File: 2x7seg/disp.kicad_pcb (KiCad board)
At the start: 2 copper layers, 35.6 x 30.5 mm, 9 parts, among them P1 CONN_01X08, P2 CONN_01X08, U1 TLC59282

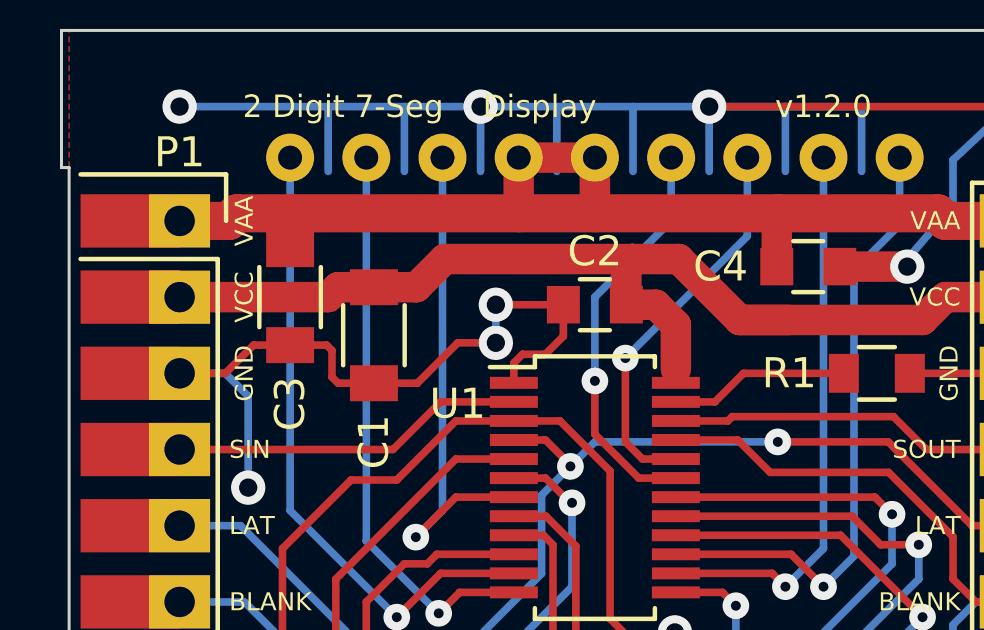
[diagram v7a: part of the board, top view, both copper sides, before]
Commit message: Move U1 reference designator. Upload to OSHPark.
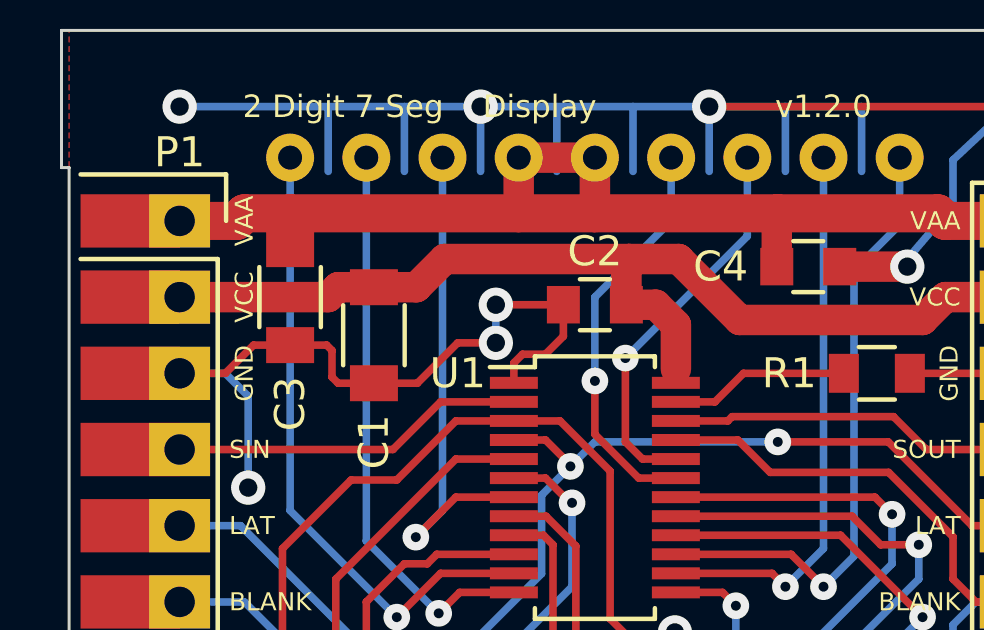
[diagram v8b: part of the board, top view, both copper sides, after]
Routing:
- net VCC: track 40.6 -> 38.9 mm
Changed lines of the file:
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@@
     (thickness 1.6)
     (drawings 35)
-    (tracks 289)
+    (tracks 286)
     (zones 0)
     (modules 9)
@@
   )
   (setup
-    (last_trace_width 0.254)
+    (last_trace_width 1.016)
     (user_trace_width 0.254)
     (user_trace_width 0.381)
@@
     (tags "SOIC 25mil")
     (attr smd)
-    (fp_text reference U1 (at -4.572 -2.794) (layer F.SilkS)
+    (fp_text reference U1 (at -4.572 -3.81) (layer F.SilkS)
       (effects (font (size 1 1) (thickness 0.15)))
     )
@@
   (gr_line (start 127 114.3) (end 162.56 114.3) (angle 90) (layer Edge.Cuts) (width 0.1))
   (gr_line (start 127.254 88.392) (end 127.254 109.728) (angle 90) (layer Edge.Cuts) (width 0.1))
+  (segment (start 139.77 91.44) (end 145.923 91.44) (width 1.016) (layer F.Cu) (net 1))
+  (segment (start 145.923 91.44) (end 147.574 91.44) (width 1.016) (layer F.Cu) (net 1))
+  (segment (start 145.83 92.964) (end 145.83 91.533) (width 1.016) (layer F.Cu) (net 1))
+  (segment (start 145.83 91.533) (end 145.923 91.44) (width 1.016) (layer F.Cu) (net 1))
+  (segment (start 137.414 92.38) (end 138.83 92.38) (width 1.016) (layer F.Cu) (net 1))
+  (segment (start 138.83 92.38) (end 139.77 91.44) (width 1.016) (layer F.Cu) (net 1))
+  (segment (start 147.574 91.44) (end 149.606 93.472) (width 1.016) (layer F.Cu) (net 1))
   (segment (start 149.606 93.472) (end 155.702 93.472) (width 1.016) (layer F.Cu) (net 1))
   (segment (start 155.702 93.472) (end 156.464 92.71) (width 1.016) (layer F.Cu) (net 1))
-  (segment (start 156.464 92.71) (end 160.655 92.71) (width 1.016) (layer F.Cu) (net 1) (status 20))
+  (segment (start 156.464 92.71) (end 160.655 92.71) (width 1.016) (layer F.Cu) (net 1))
   (segment (start 145.83 92.964) (end 146.812 92.964) (width 1.016) (layer F.Cu) (net 1) (status 10))
   (segment (start 146.812 92.964) (end 147.48 93.632) (width 1.016) (layer F.Cu) (net 1))
   (segment (start 147.48 93.632) (end 147.48 95.1135) (width 1.016) (layer F.Cu) (net 1))
-  (segment (start 145.83 92.964) (end 145.83 91.64002) (width 1.016) (layer F.Cu) (net 1) (status 10))
-  (segment (start 145.83 91.64002) (end 146.03002 91.44) (width 1.016) (layer F.Cu) (net 1))
   (segment (start 128.905 92.71) (end 135.89 92.71) (width 1.016) (layer F.Cu) (net 1) (status 10))
   (segment (start 135.89 92.71) (end 136.22 92.38) (width 1.016) (layer F.Cu) (net 1))
   (segment (start 136.22 92.38) (end 137.414 92.38) (width 1.016) (layer F.Cu) (net 1) (status 20))
-  (segment (start 137.414 92.38) (end 138.83 92.38) (width 1.016) (layer F.Cu) (net 1) (status 10))
-  (segment (start 138.83 92.38) (end 139.77 91.44) (width 1.016) (layer F.Cu) (net 1))
-  (segment (start 139.77 91.44) (end 146.02998 91.44) (width 1.016) (layer F.Cu) (net 1))
-  (segment (start 146.02998 91.44) (end 146.02999 91.44001) (width 1.016) (layer F.Cu) (net 1))
-  (segment (start 146.03001 91.44001) (end 146.03002 91.44) (width 1.016) (layer F.Cu) (net 1))
-  (segment (start 146.03002 91.44) (end 147.574 91.44) (width 1.016) (layer F.Cu) (net 1))
-  (segment (start 147.574 91.44) (end 149.606 93.472) (width 1.016) (layer F.Cu) (net 1))
-  (segment (start 149.606 93.472) (end 151.257 93.472) (width 1.016) (layer F.Cu) (net 1))
   (segment (start 147.48 95.1135) (end 147.48 95.5675) (width 0.254) (layer F.Cu) (net 1) (status 20))
   (via (at 148.59 111.76) (size 1.143) (drill 0.6096) (layers F.Cu B.Cu) (net 2))
@@
   (segment (start 156.718 88.138) (end 158.623 86.36) (width 0.254) (layer B.Cu) (net 2))
   (segment (start 155.194 91.694) (end 155.194 91.44) (width 0.254) (layer B.Cu) (net 2))
+  (segment (start 134.62 89.916) (end 133.096 89.916) (width 1.27) (layer F.Cu) (net 3))
+  (segment (start 133.096 89.916) (end 132.842 90.17) (width 1.27) (layer F.Cu) (net 3))
+  (segment (start 132.842 90.17) (end 130.937 90.17) (width 1.27) (layer F.Cu) (net 3))
+  (segment (start 156.21 89.916) (end 150.876 89.916) (width 1.27) (layer F.Cu) (net 3))
+  (segment (start 150.876 89.916) (end 144.78 89.916) (width 1.27) (layer F.Cu) (net 3))
+  (segment (start 150.842 91.694) (end 150.842 89.95) (width 1.016) (layer F.Cu) (net 3))
+  (segment (start 150.842 89.95) (end 150.876 89.916) (width 1.016) (layer F.Cu) (net 3))
   (segment (start 144.78 89.916) (end 142.24 89.916) (width 1.27) (layer F.Cu) (net 3))
   (segment (start 142.24 89.916) (end 134.62 89.916) (width 1.27) (layer F.Cu) (net 3))
   (segment (start 142.24 88.06) (end 142.24 89.916) (width 1.016) (layer F.Cu) (net 3) (status 10))
-  (segment (start 150.876 89.916) (end 144.78 89.916) (width 1.27) (layer F.Cu) (net 3))
   (segment (start 144.78 88.06) (end 144.78 89.916) (width 1.016) (layer F.Cu) (net 3) (status 10))
-  (segment (start 156.21 89.916) (end 150.876 89.916) (width 1.27) (layer F.Cu) (net 3))
-  (segment (start 150.842 91.694) (end 150.842 89.95) (width 1.016) (layer F.Cu) (net 3) (status 10))
-  (segment (start 150.842 89.95) (end 150.876 89.916) (width 1.016) (layer F.Cu) (net 3))
-  (segment (start 134.62 89.916) (end 132.842 89.916) (width 1.27) (layer F.Cu) (net 3))
   (segment (start 134.62 91.11) (end 134.62 89.916) (width 1.016) (layer F.Cu) (net 3) (status 10))
   (segment (start 158.623 90.17) (end 156.464 90.17) (width 1.27) (layer F.Cu) (net 3) (status 10))
   (segment (start 156.464 90.17) (end 156.21 89.916) (width 1.27) (layer F.Cu) (net 3))
-  (segment (start 132.842 89.916) (end 132.588 90.17) (width 1.27) (layer F.Cu) (net 3))
-  (segment (start 132.588 90.17) (end 130.937 90.17) (width 1.27) (layer F.Cu) (net 3) (status 20))
   (segment (start 144.78 88.06) (end 142.24 88.06) (width 1.016) (layer F.Cu) (net 3) (status 30))
   (via (at 150.876 97.536) (size 0.889) (drill 0.3302) (layers F.Cu B.Cu) (net 4))
